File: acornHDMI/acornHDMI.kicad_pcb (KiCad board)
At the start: 4 copper layers, 54.6 x 45.7 mm, 33 parts, among them J1 0.1" grid male, J2 8P8C_Shielded, J3 HDMI_A, U1 PTN3381D, U2 PCA9534

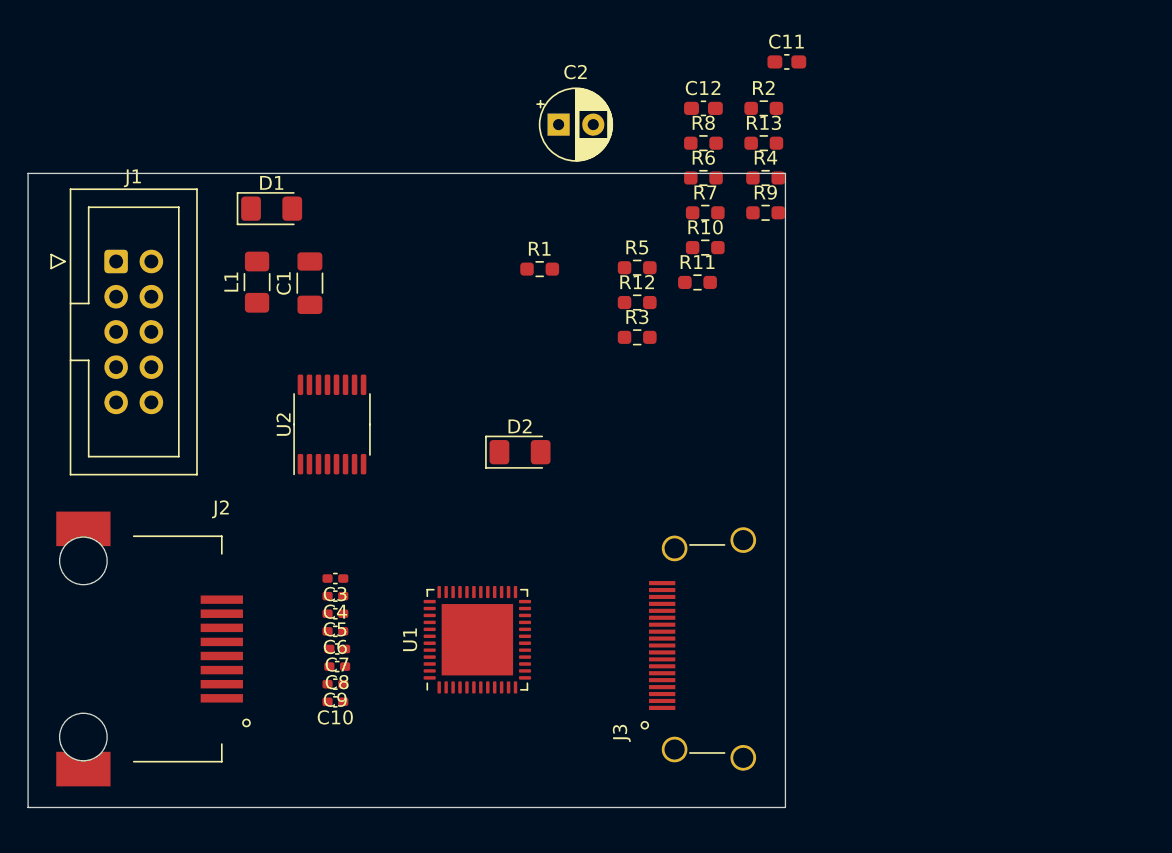
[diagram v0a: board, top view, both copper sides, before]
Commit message: change PTN3381D to B
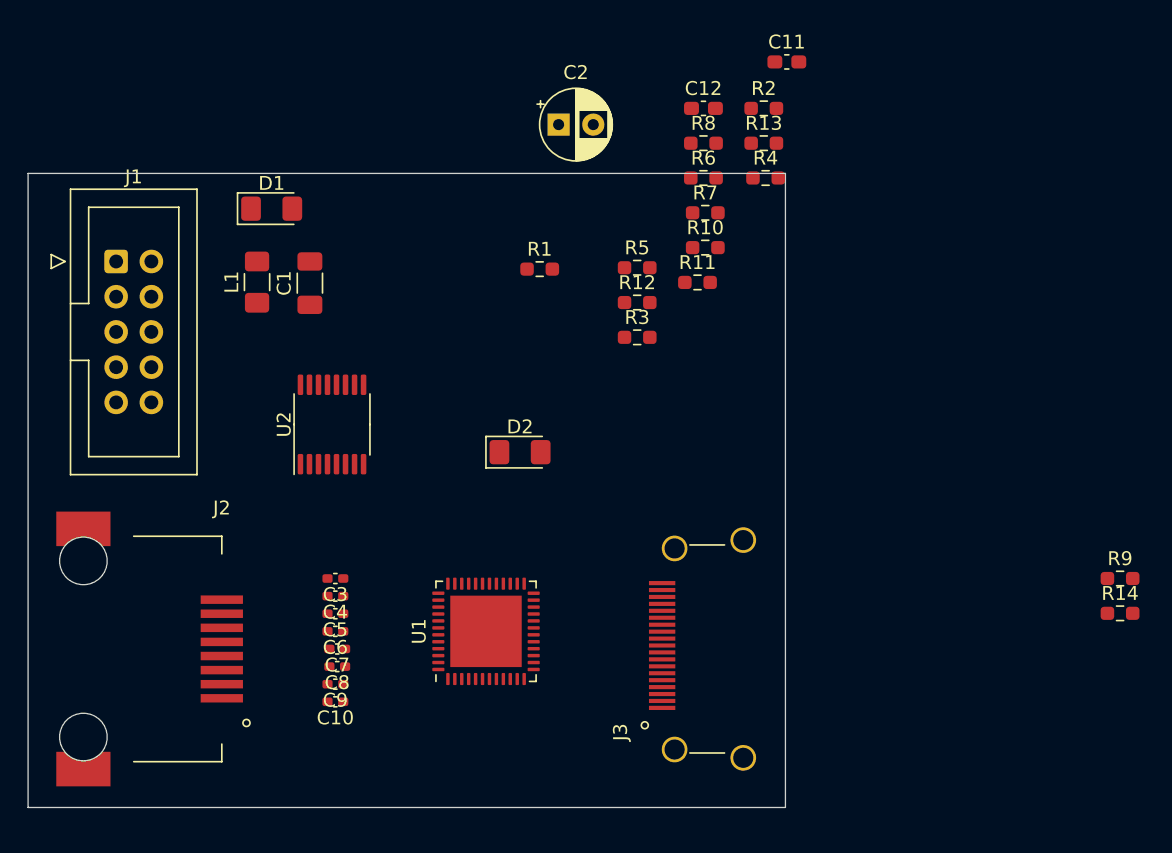
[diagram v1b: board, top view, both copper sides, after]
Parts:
- added R14: 133, Resistor_SMD:R_0603_1608Metric_Pad0.98x0.95mm_HandSolder, F.Cu at (162.6, 102.8)
- R9: value 10k -> 133
- U1: value PTN3381D -> PTN3381B
- moved R9 36.7 mm to (162.6, 100.3)
- moved U1 0.87 mm to (116.8, 104.1)
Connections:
- R11 pad 2: Net-(D2-Pad2) -> Net-(R11-Pad2)
- R9 pad 1: /EQ5 -> Net-(R9-Pad1)
- U1 pad 10: GND -> Net-(R9-Pad1)
- U1 pad 3: /EQ5 -> Net-(R11-Pad1)
- U2 pad 10: Net-(R11-Pad1) -> Net-(R14-Pad1)
- U2 pad 4: /OE_N -> Net-(R11-Pad2)
- U2 pad 5: /HPD -> Net-(R9-Pad2)
- U2 pad 6: Net-(R9-Pad2) -> /OE_N
- U2 pad 7: /EQ5 -> /HPD

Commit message: tighten up placement, start routing
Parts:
- R10, R12, R13, R2, R3, R5, R6, R7, R8: moved to B.Cu
- moved R4 45.4 mm to (115.8, 111.6), turned to 270 degrees
- moved C11 44.0 mm to (112.8, 98.8), turned to 180 degrees
- moved R2 44.0 mm to (130.7, 110.0)
- moved R7 41.3 mm to (96.0, 93.1), turned to 90 degrees
- moved R6 40.3 mm to (98.6, 93.1), turned to 90 degrees
- moved R14 38.9 mm to (127.4, 86.4)
- moved R9 38.8 mm to (124.1, 95.2), turned to 180 degrees
- moved R5 37.5 mm to (93.5, 93.1), turned to 90 degrees
- moved C12 35.5 mm to (115.0, 97.3)
- moved R8 30.8 mm to (121.8, 97.8)
- moved R13 26.1 mm to (127.5, 93.3), turned to 270 degrees
- moved R3 25.7 mm to (130.7, 108.5)
- moved C2 23.3 mm to (110.2, 87.6), turned to 90 degrees
- moved R11 20.0 mm to (120.5, 95.2)
- moved D1 19.7 mm to (116.2, 86.7), turned to 270 degrees
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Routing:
- net GND: track 0.00 -> 29.7 mm, vias 0 -> 17
- net +3V3: track 0.00 -> 17.3 mm, vias 0 -> 21
- net Net-(J1-Pad1): track 0.00 -> 11.2 mm
- net /SDA: track 0.00 -> 6.47 mm
- net /INT_N: track 0.00 -> 6.47 mm
- net Net-(R14-Pad1): track 0.00 -> 4.30 mm
- net /SCL: track 0.00 -> 3.89 mm
- net Net-(D2-Pad2): track 0.00 -> 3.08 mm
- net Net-(R4-Pad1): track 0.00 -> 2.59 mm
- net Net-(D1-Pad2): track 0.00 -> 2.12 mm
- net /OE_N: track 0.00 -> 1.89 mm
- added copper zone on F.Cu, net +3V3
- added copper zone on In2.Cu, net +3V3
- added copper zone on In1.Cu, net GND
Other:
- board size 54.6 x 45.7 mm -> 50.8 x 34.3 mm

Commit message: change to 3M 7700 cable
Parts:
- removed J2: 8P8C_Shielded, local:RJCSE-x380-01
- J1: value 0.1" grid male -> Conn_01x20_Shielded; footprint Connector_IDC:IDC-Header_2x05_P2.54mm_Vertical -> local:3M_7700_20
- moved J1 20.6 mm to (99.1, 106.9)
- moved C7 0.14 mm to (105.5, 105.9)
- moved C8 0.14 mm to (105.5, 107.2)
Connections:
- net Net-(J1-Pad1) renamed /3V3_RAW
- C10 pad 2: Net-(C10-Pad2) -> /DIO4_N
- C3 pad 2: Net-(C3-Pad2) -> /DIO3_N
- C4 pad 2: Net-(C4-Pad2) -> /DIO3_P
- C5 pad 2: Net-(C5-Pad2) -> /DIO1_N
- C6 pad 2: Net-(C6-Pad2) -> /DIO1_P
- C7 pad 2: Net-(C7-Pad2) -> /DIO2_P
- C8 pad 2: Net-(C8-Pad2) -> /DIO2_N
- C9 pad 2: Net-(C9-Pad2) -> /DIO4_P
- J1 pad 10: GND -> /DIO2_N
- J1 pad 3: /SDA -> /DIO3_N
- J1 pad 4: /SCL -> /DIO3_P
- J1 pad 5: /INT_N -> GND
- J1 pad 6: Net-(J1-Pad6) -> /DIO1_N
- J1 pad 7: GND -> /DIO1_P
- J1 pad 9: GND -> /DIO2_P
- R5 pad 2: /INT_N -> /AIO1N
- R6 pad 2: /SCL -> /AIO2N
- R7 pad 2: /SDA -> /AIO1P
- U1 pad 8: /SDA -> /AIO1P
- U1 pad 9: /SCL -> /AIO2N
- U2 pad 13: /INT_N -> /AIO1N
- U2 pad 14: /SCL -> /AIO2N
- U2 pad 15: /SDA -> /AIO1P
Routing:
- net /3V3_RAW: track 11.2 -> 0.00 mm
- net /SDA: track 6.47 -> 0.00 mm
- net /INT_N: track 6.47 -> 0.00 mm
- net /SCL: track 3.89 -> 0.00 mm

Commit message: routing in progress
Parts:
- R11, R9, U2: moved to B.Cu
- moved R14 29.4 mm to (120.0, 114.8)
- moved R10 26.9 mm to (111.0, 112.2)
- moved R13 26.1 mm to (109.5, 112.2)
- moved D2 25.7 mm to (120.9, 112.5), turned to 0 degrees
- moved R5 23.0 mm to (106.7, 111.9)
- moved U2 22.5 mm to (105.7, 104.9), turned to 270 degrees
- moved R12 21.5 mm to (114.0, 112.2)
- moved R7 20.3 mm to (103.6, 111.9)
- moved R6 20.0 mm to (105.2, 111.9)
- moved R9 19.1 mm to (105.2, 98.0), turned to 270 degrees
- moved R11 18.7 mm to (112.5, 112.2), turned to 90 degrees
- moved R8 15.1 mm to (106.7, 98.0), turned to 270 degrees
- moved L1 8.69 mm to (101.1, 95.3), turned to 270 degrees
- moved C11 1.00 mm to (111.9, 99.3)
- moved C12 0.57 mm to (115.2, 97.8)
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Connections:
- net /AIO1N renamed /INT_N
- net /AIO1P renamed /SDA
- net /AIO2N renamed /SCL
- net Net-(C12-Pad1) renamed /H_5V
- net Net-(J3-Pad1) renamed /H_D2+
- net Net-(J3-Pad10) renamed /H_CK+
- net Net-(J3-Pad12) renamed /H_CK-
- net Net-(J3-Pad15) renamed /H_SCL
- net Net-(J3-Pad16) renamed /H_SDA
- net Net-(J3-Pad19) renamed /H_HPD
- net Net-(J3-Pad3) renamed /H_D2-
- net Net-(J3-Pad4) renamed /H_D1+
- net Net-(J3-Pad6) renamed /H_D1-
- net Net-(J3-Pad7) renamed /H_D0+
- net Net-(J3-Pad9) renamed /H_D0-
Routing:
- net /H_5V: track 0.00 -> 46.8 mm, vias 0 -> 1
- net /SDA: track 0.00 -> 38.3 mm, vias 0 -> 2
- net /SCL: track 0.00 -> 34.3 mm, vias 0 -> 2
- net /H_SDA: track 0.00 -> 31.2 mm, vias 0 -> 1
- net /H_SCL: track 0.00 -> 26.0 mm, vias 0 -> 1
- net /CEC: track 0.00 -> 22.4 mm, vias 0 -> 1
- net GND: track 29.7 -> 51.2 mm, vias 17 -> 28
- net /HPD: track 0.00 -> 18.7 mm, vias 0 -> 1
- net /DDET: track 0.00 -> 14.3 mm, vias 0 -> 1
- net /INT_N: track 0.00 -> 13.5 mm, vias 0 -> 1
- net Net-(R11-Pad2): track 0.00 -> 12.2 mm
- net Net-(R14-Pad1): track 4.30 -> 15.8 mm, vias 0 -> 1
- net /H_HPD: track 0.00 -> 10.2 mm, vias 0 -> 1
- net /3V3_RAW: track 0.00 -> 8.66 mm
- net Net-(R11-Pad1): track 0.00 -> 7.03 mm, vias 0 -> 1
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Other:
- outline, holes or cut-outs redrawn
- net class diffpair added: clearance 0.1524, trace_width 0.1524, via_dia 0.4572, via_drill 0.254

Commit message: a bit of routing. need to reconsider connector
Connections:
- net Net-(C10-Pad1) renamed /PTN4_P
- net Net-(C3-Pad1) renamed /PTN1_N
- net Net-(C4-Pad1) renamed /PTN1_P
- net Net-(C5-Pad1) renamed /PTN2_N
- net Net-(C6-Pad1) renamed /PTN2_P
- net Net-(C7-Pad1) renamed /PTN3_N
- net Net-(C8-Pad1) renamed /PTN3_P
- net Net-(C9-Pad1) renamed /PTN4_N
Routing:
- net Net-(R9-Pad1): track 2.92 -> 36.0 mm
- net /H_HPD: track 10.2 -> 28.0 mm, vias 1 -> 2
- net /DDC_EN: track 6.99 -> 24.3 mm, vias 1 -> 3
- net /OE_N: track 5.01 -> 19.5 mm, vias 0 -> 1
- net /PTN4_P: track 0.00 -> 7.38 mm
- net /PTN4_N: track 0.00 -> 7.38 mm
- net /PTN1_N: track 0.00 -> 7.26 mm
- net /PTN1_P: track 0.00 -> 7.26 mm
- net /PTN3_P: track 0.00 -> 6.95 mm
- net /PTN3_N: track 0.00 -> 6.95 mm
- net /PTN2_P: track 0.00 -> 6.83 mm
- net /PTN2_N: track 0.00 -> 6.83 mm
- net +3V3: track 19.0 -> 21.6 mm, vias 20 -> 21

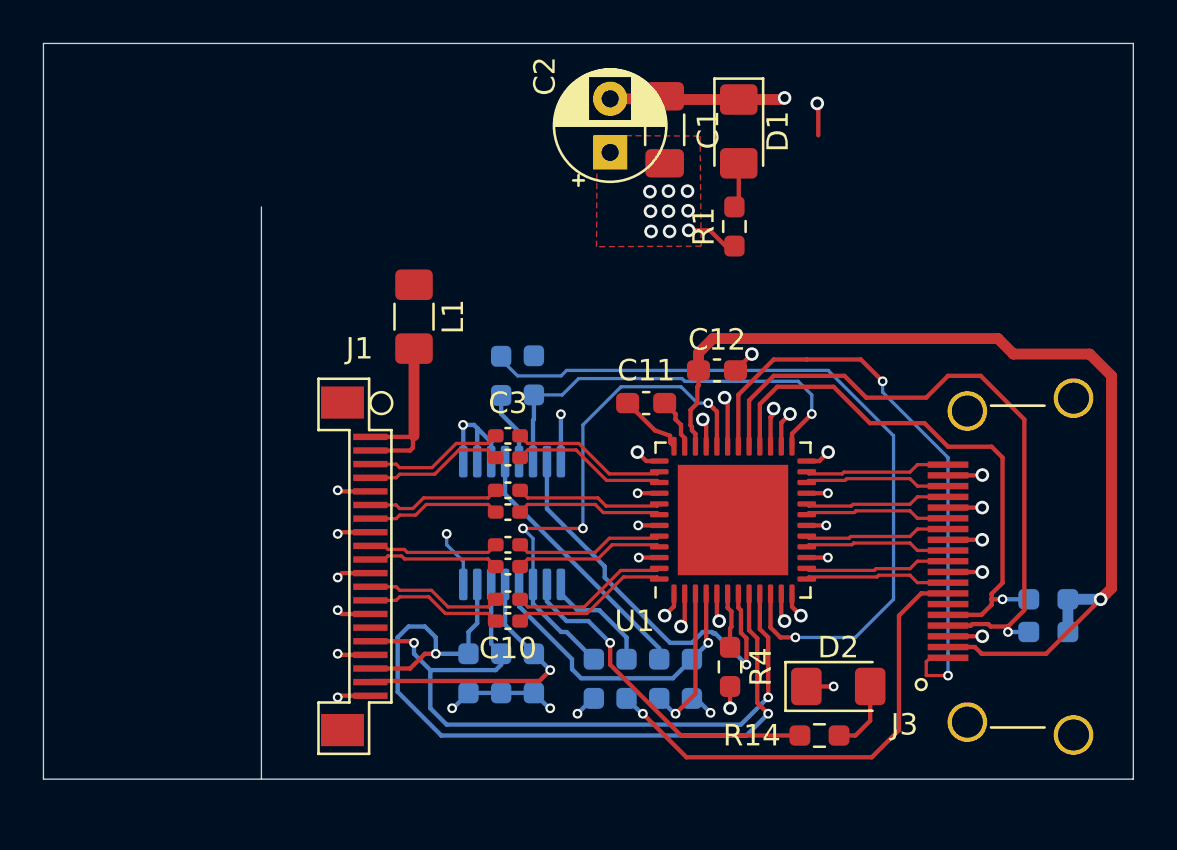
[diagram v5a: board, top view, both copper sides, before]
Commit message: add df52 to board. revise board edges, near finalization
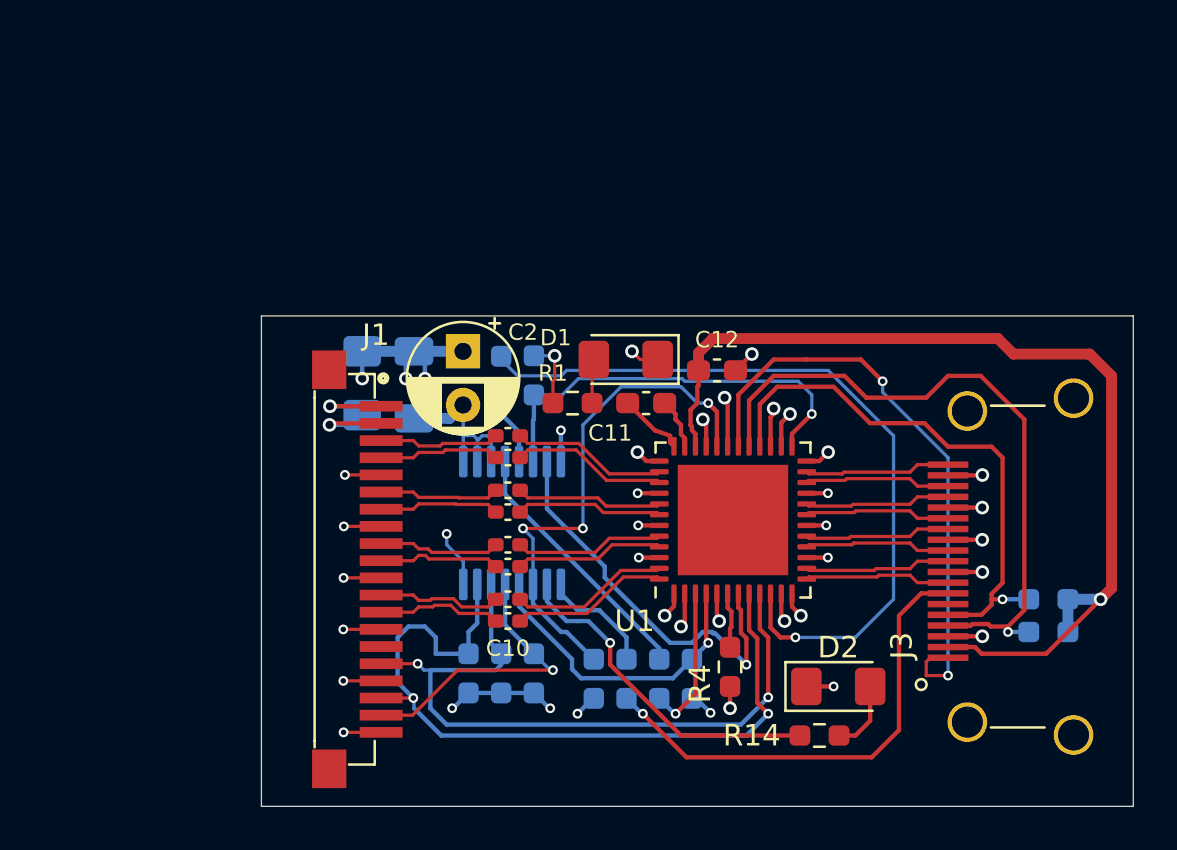
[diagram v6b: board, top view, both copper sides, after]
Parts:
- C1, L1: moved to B.Cu
- J1: footprint local:3M_7700_20 -> localfp:DF52-20-S0.8H_handsoldering
- J3: footprint local:10029449-111 -> localfp:10029449-111
- moved C1 16.7 mm to (101.1, 98.5), turned to 270 degrees
- moved D1 11.9 mm to (111.0, 97.3), turned to 180 degrees
- moved C2 11.5 mm to (103.4, 96.9), turned to 270 degrees
- moved R1 11.2 mm to (108.5, 99.3), turned to 0 degrees
- moved L1 3.93 mm to (98.7, 98.4)
- moved J1 0.14 mm to (99.1, 107.1)
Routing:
- net +3V3: track 21.6 -> 29.8 mm, vias 21 -> 15
- net GND: track 51.2 -> 47.5 mm, vias 28 -> 27
- net /SDA: track 38.3 -> 36.5 mm
- net /SCL: track 34.3 -> 33.1 mm
- net /DIO3_N: track 6.53 -> 5.64 mm
- net /DIO3_P: track 6.53 -> 5.64 mm
- net /DIO1_P: track 6.26 -> 5.60 mm
- net /DIO1_N: track 6.26 -> 5.60 mm
- net /DIO4_P: track 6.38 -> 5.78 mm
- net /DIO4_N: track 6.38 -> 5.78 mm
- net /3V3_RAW: track 8.66 -> 8.21 mm, vias 0 -> 2
- removed copper zone on F.Cu, net +3V3
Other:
- board size 50.8 x 34.3 mm -> 40.6 x 22.9 mm

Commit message: revA for initial production
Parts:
- added C13: 10n, Capacitor_SMD:C_0402_1005Metric_Pad0.74x0.62mm_HandSolder, B.Cu at (119.6, 102.6)
- added C14: 10n, Capacitor_SMD:C_0402_1005Metric_Pad0.74x0.62mm_HandSolder, B.Cu at (113.2, 108.2)
- added C15: 10n, Capacitor_SMD:C_0402_1005Metric_Pad0.74x0.62mm_HandSolder, B.Cu at (119.6, 105.9)
- added C16: 10n, Capacitor_SMD:C_0402_1005Metric_Pad0.74x0.62mm_HandSolder, B.Cu at (115.1, 101.1)
- added C17: 10n, Capacitor_SMD:C_0402_1005Metric_Pad0.74x0.62mm_HandSolder, B.Cu at (112.3, 105.9)
- added C18: 10n, Capacitor_SMD:C_0402_1005Metric_Pad0.74x0.62mm_HandSolder, B.Cu at (118.7, 108.2)
- added C19: 10n, Capacitor_SMD:C_0402_1005Metric_Pad0.74x0.62mm_HandSolder, B.Cu at (117.9, 101.1)
- added C20: 10n, Capacitor_SMD:C_0402_1005Metric_Pad0.74x0.62mm_HandSolder, B.Cu at (112.3, 102.7)
- added C21: 10n, Capacitor_SMD:C_0402_1005Metric_Pad0.74x0.62mm_HandSolder, B.Cu at (102.4, 104.1)
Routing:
- net GND: track 47.5 -> 59.4 mm, vias 27 -> 28
- net +3V3: track 29.8 -> 39.3 mm
- net /SDA: track 36.5 -> 34.3 mm
- added copper zone on B.Cu, net GND
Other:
- rule pad_to_mask_clearance: 0 -> 0.0508
- board text added: "Acorn HDMI adapter revA Nov 2021"
